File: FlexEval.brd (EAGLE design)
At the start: 94.2 x 100 mm, 182 parts, among them J1 USB4105-GF-A, J2 GRPB052VWQS-RC, SW1 1825910-7, U1 MK22FX512AVLQ12, U3 IS31FL3733B-TQLS4, U4 IS31FL3733B-TQLS4, U5 SOIC127P600X175-8N, U6 AP2115M-3.3TRG1, Y1 ABM3B-8.000MHZ-B2-T, Y2 ABS07-32.768KHZ-T

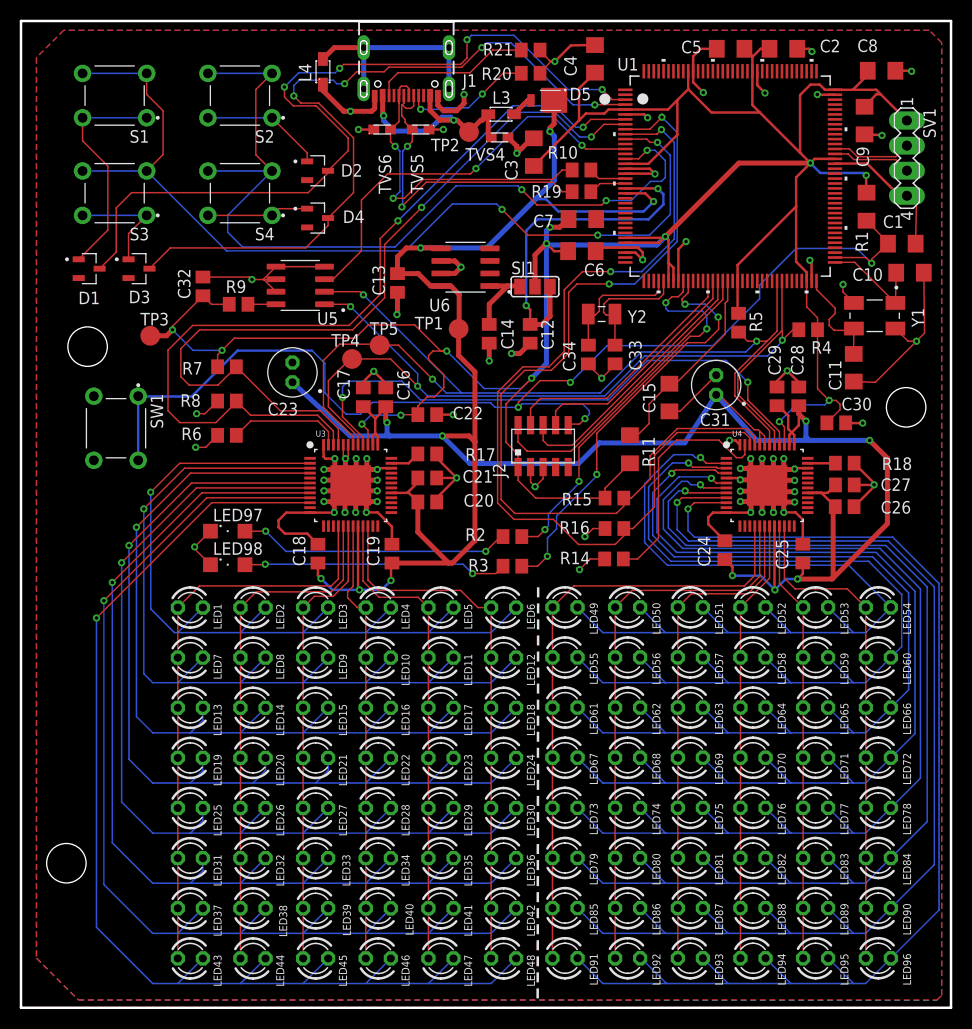
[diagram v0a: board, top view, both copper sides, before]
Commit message: board: cleaned up text locations and switched to vector fonts
Cleaned up board text locations (and added some decoration).
Switched all fonts on tNames layer to vector fonts.
Added "JLCJLCJLCJLC" to silkscreen, for JLCPCB order number
location

Signed-off-by: Daniel DeGrasse <daniel@degrasse.com>
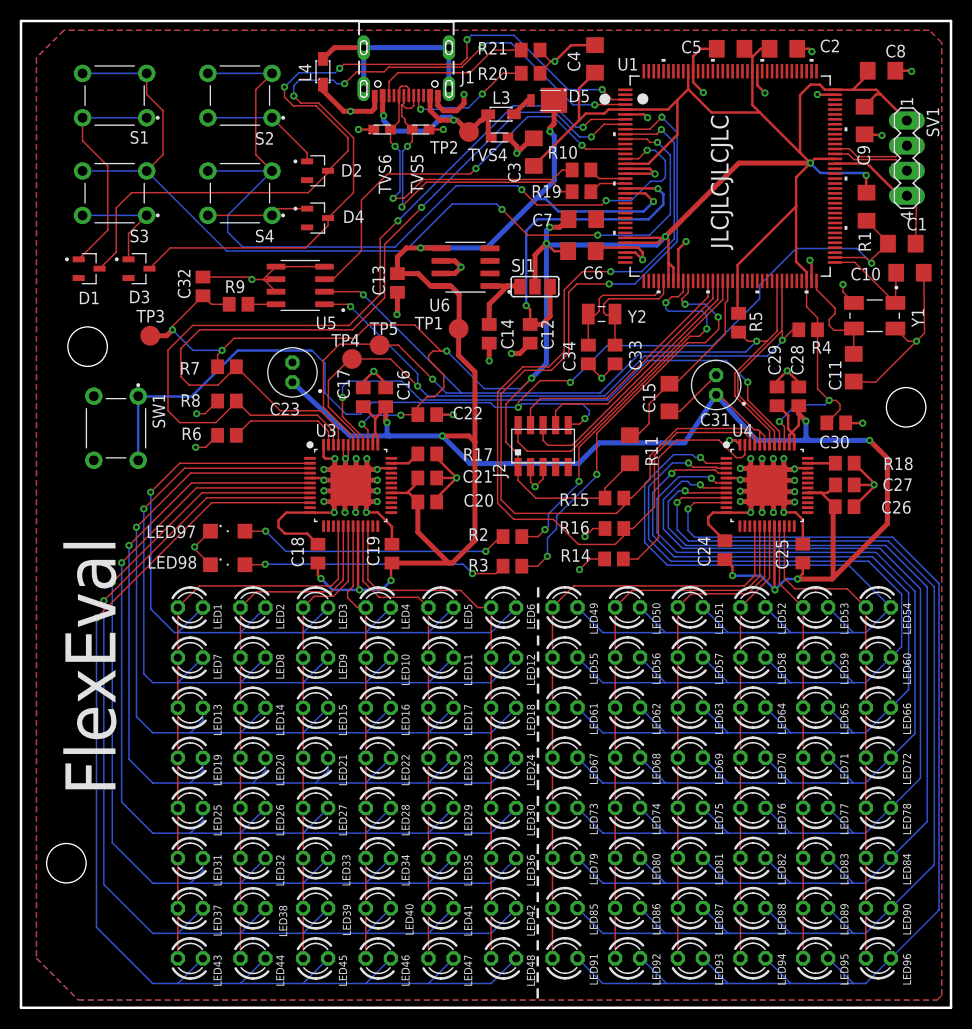
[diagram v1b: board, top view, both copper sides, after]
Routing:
- net GND: track 299.5 -> 301.0 mm
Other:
- board text added: "FlexEval"
- board text added: "JLCJLCJLCJLC"
